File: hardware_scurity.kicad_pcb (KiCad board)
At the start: 2 copper layers, 137.3 x 121 mm, 34 parts, among them J10 Screw_Terminal_01x02, J11 Conn_01x04, J12 281740-4, J13 Conn_01x04, J14 Conn_01x01_Pin, J15 Screw_Terminal_01x02, J16 Screw_Terminal_01x02, J17 Screw_Terminal_01x02, J18 Screw_Terminal_01x02, J19 Screw_Terminal_01x02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

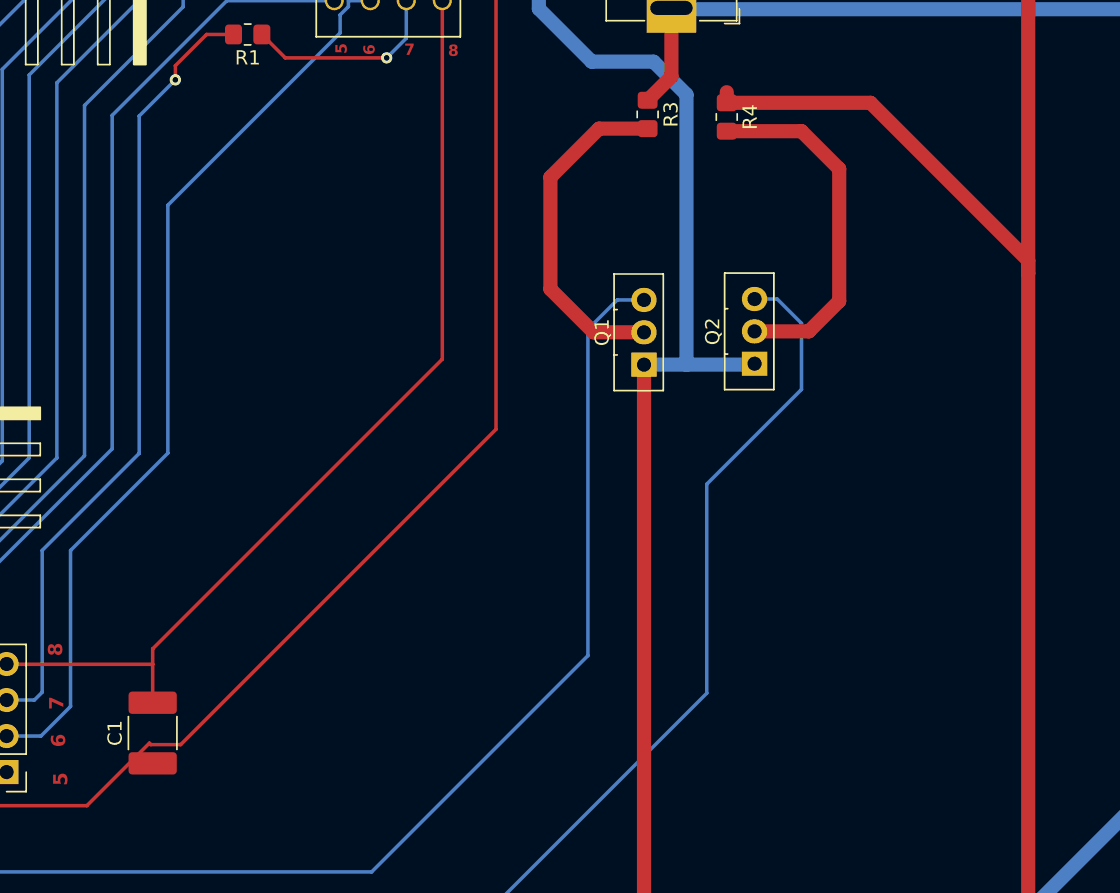
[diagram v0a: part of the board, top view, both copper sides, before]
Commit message: fix(tjoint): Change the routing.
    In the output plane there was the issue in routing which is updated
    and replace witht the t joint.

Signed-off-by: tej-dabhankar <tejasdabhankar123@gmail.com>
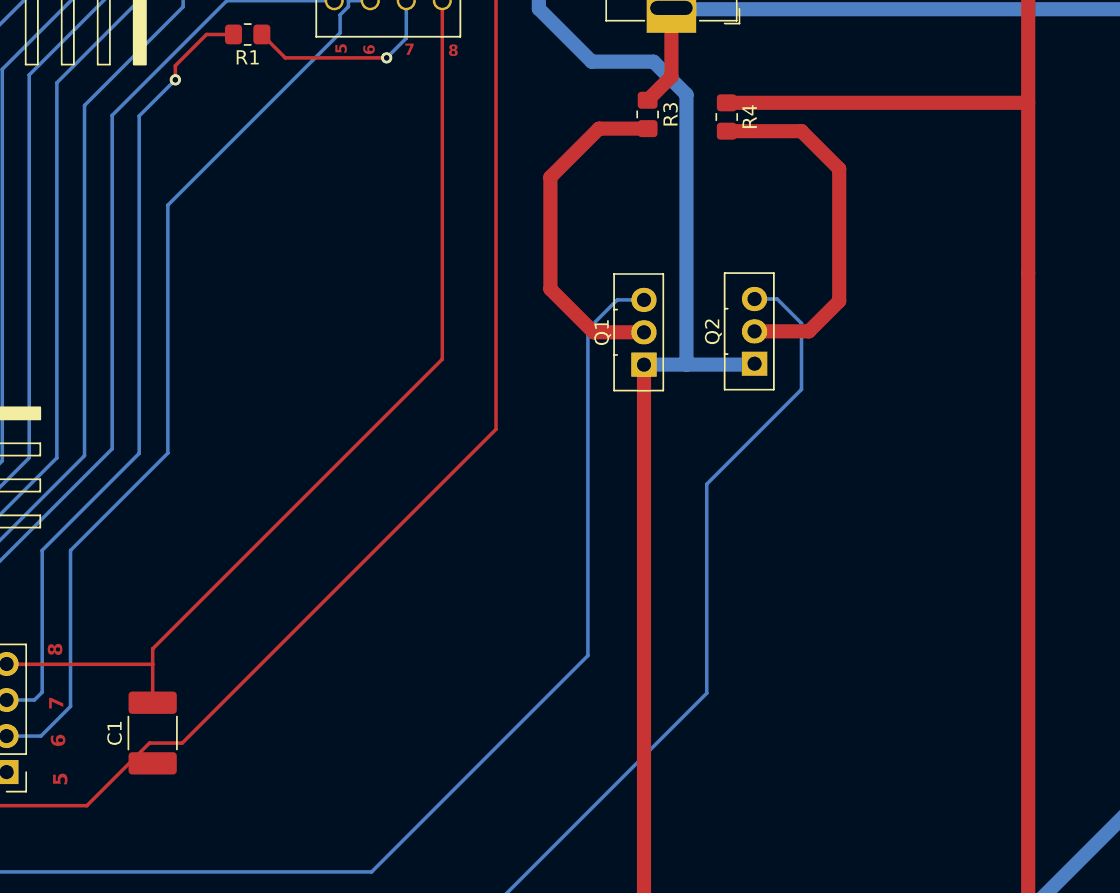
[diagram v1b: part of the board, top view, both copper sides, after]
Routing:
- net Net-(J10-Pin_1): track 144.8 -> 138.5 mm
